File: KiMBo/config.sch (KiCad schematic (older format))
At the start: 18 parts

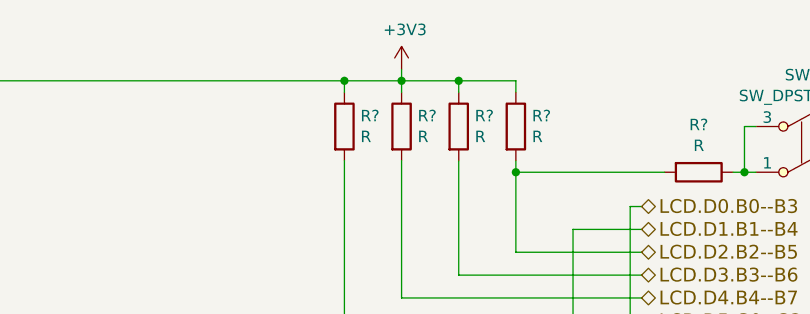
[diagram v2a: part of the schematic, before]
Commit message: Update the rest of the power rails and add two more stepper drivers
Now has *nine* stepper drivers, this will increase cost, and may drastically increase development time...
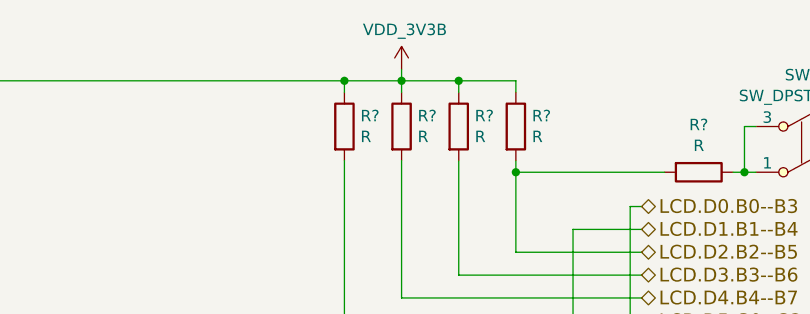
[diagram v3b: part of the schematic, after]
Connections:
- net +3V3 renamed VDD_3V3B
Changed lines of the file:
@@
 $Descr A4 11693 8268
 encoding utf-8
-Sheet 9 25
+Sheet 9 27
 Title ""
 Date ""
@@
 	1    0    0    -1
 $EndComp
-$Comp
-L +3V3 #PWR?
-U 1 1 58A2820F
-P 5900 1300
-F 0 "#PWR?" H 5900 1150 50  0001 C CNN
-F 1 "+3V3" H 5915 1473 50  0000 C CNN
-F 2 "" H 5900 1300 50  0000 C CNN
-F 3 "" H 5900 1300 50  0000 C CNN
-	1    5900 1300
-	1    0    0    -1
-$EndComp
 Wire Wire Line
 	6950 1900 6900 1900
@@
 	1    0    0    -1
 $EndComp
+$Comp
+L VDD_3V3B #PWR?
+U 1 1 5A05FAAA
+P 5900 1300
+F 0 "#PWR?" H 5900 1150 50  0001 C CNN
+F 1 "VDD_3V3B" H 5915 1473 50  0000 C CNN
+F 2 "" H 5900 1300 50  0000 C CNN
+F 3 "" H 5900 1300 50  0000 C CNN
+	1    5900 1300
+	1    0    0    -1
+$EndComp

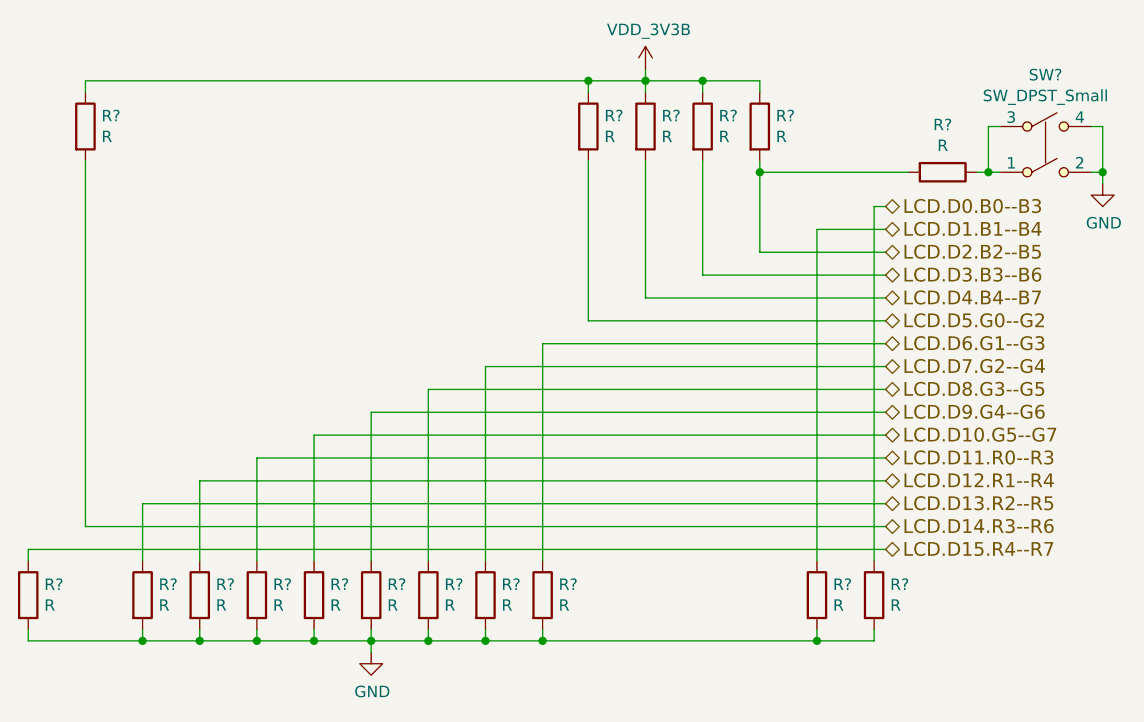
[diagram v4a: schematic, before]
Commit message: Show which components are DNP, begin spec of components, and refine the power input circuit
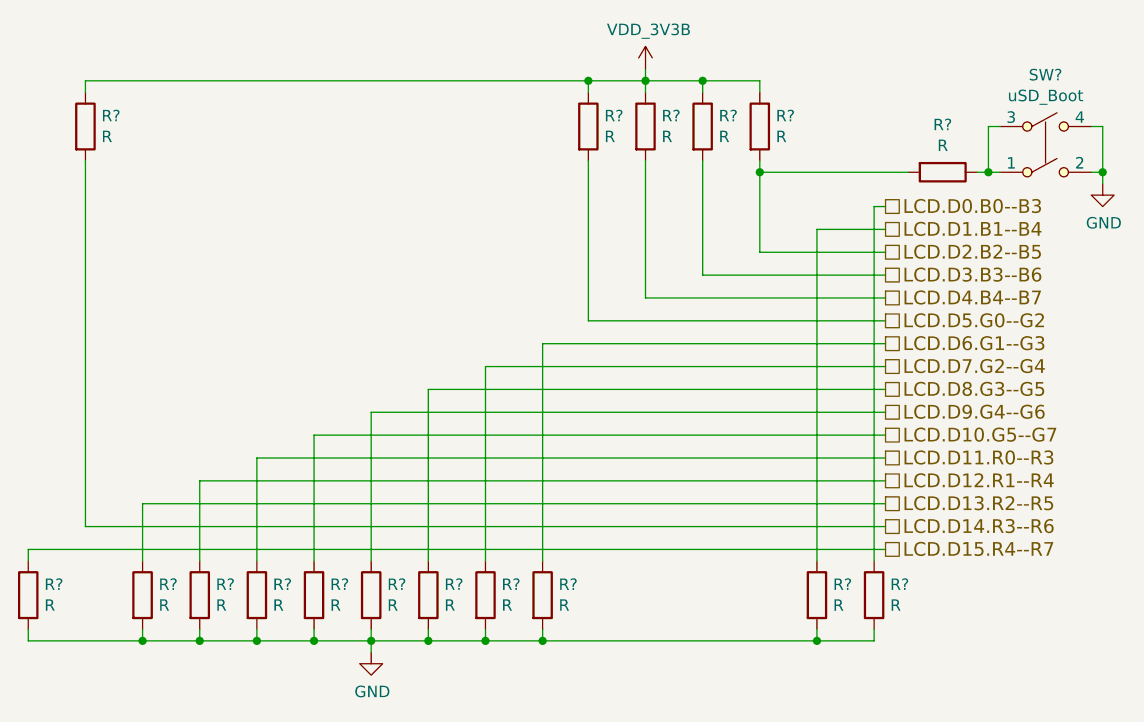
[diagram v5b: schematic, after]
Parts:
- SW?: value SW_DPST_Small -> uSD_Boot
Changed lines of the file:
@@
 $Descr A4 11693 8268
 encoding utf-8
-Sheet 9 26
+Sheet 16 26
 Title ""
 Date ""
@@
 U 1 1 58A2324A
 P 4200 3600
+AR Path="/589C2BEE/58A2324A" Ref="R?"  Part="1"
+AR Path="/58958D2E/5AD44766/58A2324A" Ref="R?"  Part="1"
 F 0 "R?" H 4270 3646 50  0000 L CNN
 F 1 "R" H 4270 3555 50  0000 L CNN
@@
 U 1 1 58A2326A
 P 4450 3600
+AR Path="/589C2BEE/58A2326A" Ref="R?"  Part="1"
+AR Path="/58958D2E/5AD44766/58A2326A" Ref="R?"  Part="1"
 F 0 "R?" H 4520 3646 50  0000 L CNN
 F 1 "R" H 4520 3555 50  0000 L CNN
@@
 U 1 1 58A2328E
 P 4700 3600
+AR Path="/589C2BEE/58A2328E" Ref="R?"  Part="1"
+AR Path="/58958D2E/5AD44766/58A2328E" Ref="R?"  Part="1"
 F 0 "R?" H 4770 3646 50  0000 L CNN
 F 1 "R" H 4770 3555 50  0000 L CNN
@@
 U 1 1 58A232B1
 P 4950 3600
+AR Path="/589C2BEE/58A232B1" Ref="R?"  Part="1"
+AR Path="/58958D2E/5AD44766/58A232B1" Ref="R?"  Part="1"
 F 0 "R?" H 5020 3646 50  0000 L CNN
 F 1 "R" H 5020 3555 50  0000 L CNN
@@
 U 1 1 58A232DB
 P 5200 3600
+AR Path="/589C2BEE/58A232DB" Ref="R?"  Part="1"
+AR Path="/58958D2E/5AD44766/58A232DB" Ref="R?"  Part="1"
 F 0 "R?" H 5270 3646 50  0000 L CNN
 F 1 "R" H 5270 3555 50  0000 L CNN
@@
 U 1 1 58A23304
 P 5450 3600
+AR Path="/589C2BEE/58A23304" Ref="R?"  Part="1"
+AR Path="/58958D2E/5AD44766/58A23304" Ref="R?"  Part="1"
 F 0 "R?" H 5520 3646 50  0000 L CNN
 F 1 "R" H 5520 3555 50  0000 L CNN
@@
 U 1 1 58A23332
 P 6650 3600
+AR Path="/589C2BEE/58A23332" Ref="R?"  Part="1"
+AR Path="/58958D2E/5AD44766/58A23332" Ref="R?"  Part="1"
 F 0 "R?" H 6720 3646 50  0000 L CNN
 F 1 "R" H 6720 3555 50  0000 L CNN
@@
 U 1 1 58A23361
 P 6900 3600
+AR Path="/589C2BEE/58A23361" Ref="R?"  Part="1"
+AR Path="/58958D2E/5AD44766/58A23361" Ref="R?"  Part="1"
 F 0 "R?" H 6970 3646 50  0000 L CNN
 F 1 "R" H 6970 3555 50  0000 L CNN
@@
 	1    0    0    -1
 $EndComp
-Text HLabel 6950 1900 2    60   BiDi ~ 0
+Text HLabel 6950 1900 2    60   UnSpc ~ 0
 LCD.D0.B0--B3
-Text HLabel 6950 2000 2    60   BiDi ~ 0
+Text HLabel 6950 2000 2    60   UnSpc ~ 0
 LCD.D1.B1--B4
-Text HLabel 6950 2100 2    60   BiDi ~ 0
+Text HLabel 6950 2100 2    60   UnSpc ~ 0
 LCD.D2.B2--B5
-Text HLabel 6950 2200 2    60   BiDi ~ 0
+Text HLabel 6950 2200 2    60   UnSpc ~ 0
 LCD.D3.B3--B6
-Text HLabel 6950 2300 2    60   BiDi ~ 0
+Text HLabel 6950 2300 2    60   UnSpc ~ 0
 LCD.D4.B4--B7
-Text HLabel 6950 2400 2    60   BiDi ~ 0
+Text HLabel 6950 2400 2    60   UnSpc ~ 0
 LCD.D5.G0--G2
-Text HLabel 6950 2500 2    60   BiDi ~ 0
+Text HLabel 6950 2500 2    60   UnSpc ~ 0
 LCD.D6.G1--G3
-Text HLabel 6950 2600 2    60   BiDi ~ 0
+Text HLabel 6950 2600 2    60   UnSpc ~ 0
 LCD.D7.G2--G4
-Text HLabel 6950 2700 2    60   BiDi ~ 0
+Text HLabel 6950 2700 2    60   UnSpc ~ 0
 LCD.D8.G3--G5
-Text HLabel 6950 2800 2    60   BiDi ~ 0
+Text HLabel 6950 2800 2    60   UnSpc ~ 0
 LCD.D9.G4--G6
-Text HLabel 6950 2900 2    60   BiDi ~ 0
+Text HLabel 6950 2900 2    60   UnSpc ~ 0
 LCD.D10.G5--G7
-Text HLabel 6950 3100 2    60   BiDi ~ 0
+Text HLabel 6950 3100 2    60   UnSpc ~ 0
 LCD.D12.R1--R4
-Text HLabel 6950 3200 2    60   BiDi ~ 0
+Text HLabel 6950 3200 2    60   UnSpc ~ 0
 LCD.D13.R2--R5
-Text HLabel 6950 3300 2    60   BiDi ~ 0
+Text HLabel 6950 3300 2    60   UnSpc ~ 0
 LCD.D14.R3--R6
-Text HLabel 6950 3400 2    60   BiDi ~ 0
+Text HLabel 6950 3400 2    60   UnSpc ~ 0
 LCD.D15.R4--R7
-Text HLabel 6950 3000 2    60   BiDi ~ 0
+Text HLabel 6950 3000 2    60   UnSpc ~ 0
 LCD.D11.R0--R3
 $Comp
@@
 U 1 1 58A25F63
 P 3950 3600
+AR Path="/589C2BEE/58A25F63" Ref="R?"  Part="1"
+AR Path="/58958D2E/5AD44766/58A25F63" Ref="R?"  Part="1"
 F 0 "R?" H 4020 3646 50  0000 L CNN
 F 1 "R" H 4020 3555 50  0000 L CNN
@@
 U 1 1 58A25F94
 P 3700 3600
+AR Path="/589C2BEE/58A25F94" Ref="R?"  Part="1"
+AR Path="/58958D2E/5AD44766/58A25F94" Ref="R?"  Part="1"
 F 0 "R?" H 3770 3646 50  0000 L CNN
 F 1 "R" H 3770 3555 50  0000 L CNN
@@
 U 1 1 58A260DB
 P 3200 3600
+AR Path="/589C2BEE/58A260DB" Ref="R?"  Part="1"
+AR Path="/58958D2E/5AD44766/58A260DB" Ref="R?"  Part="1"
 F 0 "R?" H 3270 3646 50  0000 L CNN
 F 1 "R" H 3270 3555 50  0000 L CNN
@@
 U 1 1 58A262E3
 P 4700 3850
+AR Path="/589C2BEE/58A262E3" Ref="#PWR?"  Part="1"
+AR Path="/58958D2E/5AD44766/58A262E3" Ref="#PWR?"  Part="1"
 F 0 "#PWR?" H 4700 3600 50  0001 C CNN
 F 1 "GND" H 4705 3677 50  0000 C CNN
@@
 U 1 1 58A26A66
 P 6400 1550
+AR Path="/589C2BEE/58A26A66" Ref="R?"  Part="1"
+AR Path="/58958D2E/5AD44766/58A26A66" Ref="R?"  Part="1"
 F 0 "R?" H 6470 1596 50  0000 L CNN
 F 1 "R" H 6470 1505 50  0000 L CNN
@@
 U 1 1 58A26AC4
 P 6150 1550
+AR Path="/589C2BEE/58A26AC4" Ref="R?"  Part="1"
+AR Path="/58958D2E/5AD44766/58A26AC4" Ref="R?"  Part="1"
 F 0 "R?" H 6220 1596 50  0000 L CNN
 F 1 "R" H 6220 1505 50  0000 L CNN
@@
 U 1 1 58A26B05
 P 5900 1550
+AR Path="/589C2BEE/58A26B05" Ref="R?"  Part="1"
+AR Path="/58958D2E/5AD44766/58A26B05" Ref="R?"  Part="1"
 F 0 "R?" H 5970 1596 50  0000 L CNN
 F 1 "R" H 5970 1505 50  0000 L CNN
@@
 U 1 1 58A26B4F
 P 5650 1550
+AR Path="/589C2BEE/58A26B4F" Ref="R?"  Part="1"
+AR Path="/58958D2E/5AD44766/58A26B4F" Ref="R?"  Part="1"
 F 0 "R?" H 5720 1596 50  0000 L CNN
 F 1 "R" H 5720 1505 50  0000 L CNN
@@
 U 1 1 58A26BA2
 P 3450 1550
+AR Path="/589C2BEE/58A26BA2" Ref="R?"  Part="1"
+AR Path="/58958D2E/5AD44766/58A26BA2" Ref="R?"  Part="1"
 F 0 "R?" H 3520 1596 50  0000 L CNN
 F 1 "R" H 3520 1505 50  0000 L CNN
@@
 U 1 1 58A2A28E
 P 7200 1750
+AR Path="/589C2BEE/58A2A28E" Ref="R?"  Part="1"
+AR Path="/58958D2E/5AD44766/58A2A28E" Ref="R?"  Part="1"
 F 0 "R?" V 6993 1750 50  0000 C CNN
 F 1 "R" V 7084 1750 50  0000 C CNN
@@
 U 1 1 58A2A610
 P 7650 1650
+AR Path="/589C2BEE/58A2A610" Ref="SW?"  Part="1"
+AR Path="/58958D2E/5AD44766/58A2A610" Ref="SW?"  Part="1"
 F 0 "SW?" H 7650 1975 50  0000 C CNN
-F 1 "SW_DPST_Small" H 7650 1884 50  0000 C CNN
+F 1 "uSD_Boot" H 7650 1884 50  0000 C CNN
 F 2 "" H 7650 1650 50  0000 C CNN
 F 3 "" H 7650 1650 50  0000 C CNN
@@
 U 1 1 58A2A814
 P 7900 1800
+AR Path="/589C2BEE/58A2A814" Ref="#PWR?"  Part="1"
+AR Path="/58958D2E/5AD44766/58A2A814" Ref="#PWR?"  Part="1"
 F 0 "#PWR?" H 7900 1550 50  0001 C CNN
 F 1 "GND" H 7905 1627 50  0000 C CNN
@@
 U 1 1 5A05FAAA
 P 5900 1300
+AR Path="/589C2BEE/5A05FAAA" Ref="#PWR?"  Part="1"
+AR Path="/58958D2E/5AD44766/5A05FAAA" Ref="#PWR?"  Part="1"
 F 0 "#PWR?" H 5900 1150 50  0001 C CNN
 F 1 "VDD_3V3B" H 5915 1473 50  0000 C CNN

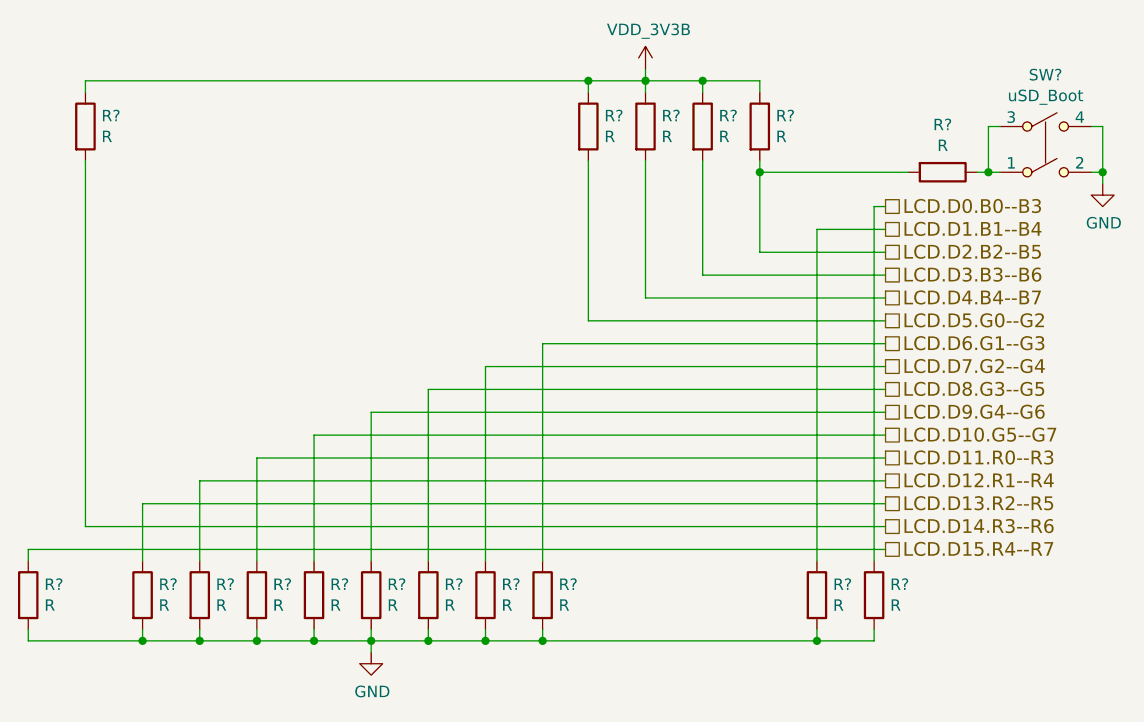
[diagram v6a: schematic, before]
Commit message: Annotate all components, now passing ERC, added ferrites to the rest of the connectors
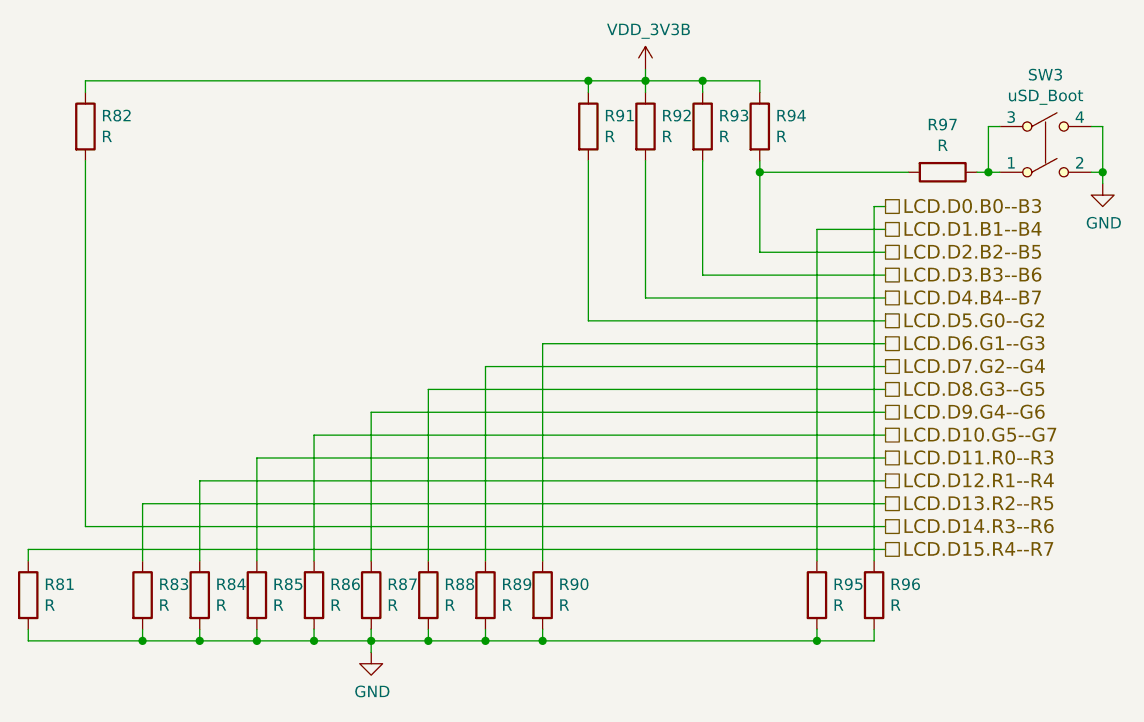
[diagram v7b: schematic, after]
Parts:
- gave numbers to parts that had none: 18
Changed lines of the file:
@@
 $Descr A4 11693 8268
 encoding utf-8
-Sheet 16 26
+Sheet 12 26
 Title ""
 Date ""
@@
 P 4200 3600
 AR Path="/589C2BEE/58A2324A" Ref="R?"  Part="1"
-AR Path="/58958D2E/5AD44766/58A2324A" Ref="R?"  Part="1"
-F 0 "R?" H 4270 3646 50  0000 L CNN
+AR Path="/58958D2E/5AD44766/58A2324A" Ref="R85"  Part="1"
+F 0 "R85" H 4270 3646 50  0000 L CNN
 F 1 "R" H 4270 3555 50  0000 L CNN
 F 2 "" V 4130 3600 50  0000 C CNN
@@
 P 4450 3600
 AR Path="/589C2BEE/58A2326A" Ref="R?"  Part="1"
-AR Path="/58958D2E/5AD44766/58A2326A" Ref="R?"  Part="1"
-F 0 "R?" H 4520 3646 50  0000 L CNN
+AR Path="/58958D2E/5AD44766/58A2326A" Ref="R86"  Part="1"
+F 0 "R86" H 4520 3646 50  0000 L CNN
 F 1 "R" H 4520 3555 50  0000 L CNN
 F 2 "" V 4380 3600 50  0000 C CNN
@@
 P 4700 3600
 AR Path="/589C2BEE/58A2328E" Ref="R?"  Part="1"
-AR Path="/58958D2E/5AD44766/58A2328E" Ref="R?"  Part="1"
-F 0 "R?" H 4770 3646 50  0000 L CNN
+AR Path="/58958D2E/5AD44766/58A2328E" Ref="R87"  Part="1"
+F 0 "R87" H 4770 3646 50  0000 L CNN
 F 1 "R" H 4770 3555 50  0000 L CNN
 F 2 "" V 4630 3600 50  0000 C CNN
@@
 P 4950 3600
 AR Path="/589C2BEE/58A232B1" Ref="R?"  Part="1"
-AR Path="/58958D2E/5AD44766/58A232B1" Ref="R?"  Part="1"
-F 0 "R?" H 5020 3646 50  0000 L CNN
+AR Path="/58958D2E/5AD44766/58A232B1" Ref="R88"  Part="1"
+F 0 "R88" H 5020 3646 50  0000 L CNN
 F 1 "R" H 5020 3555 50  0000 L CNN
 F 2 "" V 4880 3600 50  0000 C CNN
@@
 P 5200 3600
 AR Path="/589C2BEE/58A232DB" Ref="R?"  Part="1"
-AR Path="/58958D2E/5AD44766/58A232DB" Ref="R?"  Part="1"
-F 0 "R?" H 5270 3646 50  0000 L CNN
+AR Path="/58958D2E/5AD44766/58A232DB" Ref="R89"  Part="1"
+F 0 "R89" H 5270 3646 50  0000 L CNN
 F 1 "R" H 5270 3555 50  0000 L CNN
 F 2 "" V 5130 3600 50  0000 C CNN
@@
 P 5450 3600
 AR Path="/589C2BEE/58A23304" Ref="R?"  Part="1"
-AR Path="/58958D2E/5AD44766/58A23304" Ref="R?"  Part="1"
-F 0 "R?" H 5520 3646 50  0000 L CNN
+AR Path="/58958D2E/5AD44766/58A23304" Ref="R90"  Part="1"
+F 0 "R90" H 5520 3646 50  0000 L CNN
 F 1 "R" H 5520 3555 50  0000 L CNN
 F 2 "" V 5380 3600 50  0000 C CNN
@@
 P 6650 3600
 AR Path="/589C2BEE/58A23332" Ref="R?"  Part="1"
-AR Path="/58958D2E/5AD44766/58A23332" Ref="R?"  Part="1"
-F 0 "R?" H 6720 3646 50  0000 L CNN
+AR Path="/58958D2E/5AD44766/58A23332" Ref="R95"  Part="1"
+F 0 "R95" H 6720 3646 50  0000 L CNN
 F 1 "R" H 6720 3555 50  0000 L CNN
 F 2 "" V 6580 3600 50  0000 C CNN
@@
 P 6900 3600
 AR Path="/589C2BEE/58A23361" Ref="R?"  Part="1"
-AR Path="/58958D2E/5AD44766/58A23361" Ref="R?"  Part="1"
-F 0 "R?" H 6970 3646 50  0000 L CNN
+AR Path="/58958D2E/5AD44766/58A23361" Ref="R96"  Part="1"
+F 0 "R96" H 6970 3646 50  0000 L CNN
 F 1 "R" H 6970 3555 50  0000 L CNN
 F 2 "" V 6830 3600 50  0000 C CNN
@@
 P 3950 3600
 AR Path="/589C2BEE/58A25F63" Ref="R?"  Part="1"
-AR Path="/58958D2E/5AD44766/58A25F63" Ref="R?"  Part="1"
-F 0 "R?" H 4020 3646 50  0000 L CNN
+AR Path="/58958D2E/5AD44766/58A25F63" Ref="R84"  Part="1"
+F 0 "R84" H 4020 3646 50  0000 L CNN
 F 1 "R" H 4020 3555 50  0000 L CNN
 F 2 "" V 3880 3600 50  0000 C CNN
@@
 P 3700 3600
 AR Path="/589C2BEE/58A25F94" Ref="R?"  Part="1"
-AR Path="/58958D2E/5AD44766/58A25F94" Ref="R?"  Part="1"
-F 0 "R?" H 3770 3646 50  0000 L CNN
+AR Path="/58958D2E/5AD44766/58A25F94" Ref="R83"  Part="1"
+F 0 "R83" H 3770 3646 50  0000 L CNN
 F 1 "R" H 3770 3555 50  0000 L CNN
 F 2 "" V 3630 3600 50  0000 C CNN
@@
 P 3200 3600
 AR Path="/589C2BEE/58A260DB" Ref="R?"  Part="1"
-AR Path="/58958D2E/5AD44766/58A260DB" Ref="R?"  Part="1"
-F 0 "R?" H 3270 3646 50  0000 L CNN
+AR Path="/58958D2E/5AD44766/58A260DB" Ref="R81"  Part="1"
+F 0 "R81" H 3270 3646 50  0000 L CNN
 F 1 "R" H 3270 3555 50  0000 L CNN
 F 2 "" V 3130 3600 50  0000 C CNN
@@
 P 4700 3850
 AR Path="/589C2BEE/58A262E3" Ref="#PWR?"  Part="1"
-AR Path="/58958D2E/5AD44766/58A262E3" Ref="#PWR0163"  Part="1"
-F 0 "#PWR0163" H 4700 3600 50  0001 C CNN
+AR Path="/58958D2E/5AD44766/58A262E3" Ref="#PWR0172"  Part="1"
+F 0 "#PWR0172" H 4700 3600 50  0001 C CNN
 F 1 "GND" H 4705 3677 50  0000 C CNN
 F 2 "" H 4700 3850 50  0000 C CNN
@@
 P 6400 1550
 AR Path="/589C2BEE/58A26A66" Ref="R?"  Part="1"
-AR Path="/58958D2E/5AD44766/58A26A66" Ref="R?"  Part="1"
-F 0 "R?" H 6470 1596 50  0000 L CNN
+AR Path="/58958D2E/5AD44766/58A26A66" Ref="R94"  Part="1"
+F 0 "R94" H 6470 1596 50  0000 L CNN
 F 1 "R" H 6470 1505 50  0000 L CNN
 F 2 "" V 6330 1550 50  0000 C CNN
@@
 P 6150 1550
 AR Path="/589C2BEE/58A26AC4" Ref="R?"  Part="1"
-AR Path="/58958D2E/5AD44766/58A26AC4" Ref="R?"  Part="1"
-F 0 "R?" H 6220 1596 50  0000 L CNN
+AR Path="/58958D2E/5AD44766/58A26AC4" Ref="R93"  Part="1"
+F 0 "R93" H 6220 1596 50  0000 L CNN
 F 1 "R" H 6220 1505 50  0000 L CNN
 F 2 "" V 6080 1550 50  0000 C CNN
@@
 P 5900 1550
 AR Path="/589C2BEE/58A26B05" Ref="R?"  Part="1"
-AR Path="/58958D2E/5AD44766/58A26B05" Ref="R?"  Part="1"
-F 0 "R?" H 5970 1596 50  0000 L CNN
+AR Path="/58958D2E/5AD44766/58A26B05" Ref="R92"  Part="1"
+F 0 "R92" H 5970 1596 50  0000 L CNN
 F 1 "R" H 5970 1505 50  0000 L CNN
 F 2 "" V 5830 1550 50  0000 C CNN
@@
 P 5650 1550
 AR Path="/589C2BEE/58A26B4F" Ref="R?"  Part="1"
-AR Path="/58958D2E/5AD44766/58A26B4F" Ref="R?"  Part="1"
-F 0 "R?" H 5720 1596 50  0000 L CNN
+AR Path="/58958D2E/5AD44766/58A26B4F" Ref="R91"  Part="1"
+F 0 "R91" H 5720 1596 50  0000 L CNN
 F 1 "R" H 5720 1505 50  0000 L CNN
 F 2 "" V 5580 1550 50  0000 C CNN
@@
 P 3450 1550
 AR Path="/589C2BEE/58A26BA2" Ref="R?"  Part="1"
-AR Path="/58958D2E/5AD44766/58A26BA2" Ref="R?"  Part="1"
-F 0 "R?" H 3520 1596 50  0000 L CNN
+AR Path="/58958D2E/5AD44766/58A26BA2" Ref="R82"  Part="1"
+F 0 "R82" H 3520 1596 50  0000 L CNN
 F 1 "R" H 3520 1505 50  0000 L CNN
 F 2 "" V 3380 1550 50  0000 C CNN
@@
 P 7200 1750
 AR Path="/589C2BEE/58A2A28E" Ref="R?"  Part="1"
-AR Path="/58958D2E/5AD44766/58A2A28E" Ref="R?"  Part="1"
-F 0 "R?" V 6993 1750 50  0000 C CNN
+AR Path="/58958D2E/5AD44766/58A2A28E" Ref="R97"  Part="1"
+F 0 "R97" V 6993 1750 50  0000 C CNN
 F 1 "R" V 7084 1750 50  0000 C CNN
 F 2 "" V 7130 1750 50  0000 C CNN
@@
 P 7650 1650
 AR Path="/589C2BEE/58A2A610" Ref="SW?"  Part="1"
-AR Path="/58958D2E/5AD44766/58A2A610" Ref="SW?"  Part="1"
-F 0 "SW?" H 7650 1975 50  0000 C CNN
+AR Path="/58958D2E/5AD44766/58A2A610" Ref="SW3"  Part="1"
+F 0 "SW3" H 7650 1975 50  0000 C CNN
 F 1 "uSD_Boot" H 7650 1884 50  0000 C CNN
 F 2 "" H 7650 1650 50  0000 C CNN
@@
 P 7900 1800
 AR Path="/589C2BEE/58A2A814" Ref="#PWR?"  Part="1"
-AR Path="/58958D2E/5AD44766/58A2A814" Ref="#PWR0164"  Part="1"
-F 0 "#PWR0164" H 7900 1550 50  0001 C CNN
+AR Path="/58958D2E/5AD44766/58A2A814" Ref="#PWR0173"  Part="1"
+F 0 "#PWR0173" H 7900 1550 50  0001 C CNN
 F 1 "GND" H 7905 1627 50  0000 C CNN
 F 2 "" H 7900 1800 50  0000 C CNN
@@
 P 5900 1300
 AR Path="/589C2BEE/5A05FAAA" Ref="#PWR?"  Part="1"
-AR Path="/58958D2E/5AD44766/5A05FAAA" Ref="#PWR0165"  Part="1"
-F 0 "#PWR0165" H 5900 1150 50  0001 C CNN
+AR Path="/58958D2E/5AD44766/5A05FAAA" Ref="#PWR0174"  Part="1"
+F 0 "#PWR0174" H 5900 1150 50  0001 C CNN
 F 1 "VDD_3V3B" H 5915 1473 50  0000 C CNN
 F 2 "" H 5900 1300 50  0000 C CNN
